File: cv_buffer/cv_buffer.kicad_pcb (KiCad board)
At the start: 2 copper layers, 30 x 8 mm, 8 parts, among them J1 CV connector, J2 Pot connector, U1 HT7550-1, U2 TLV6001UIDBVR

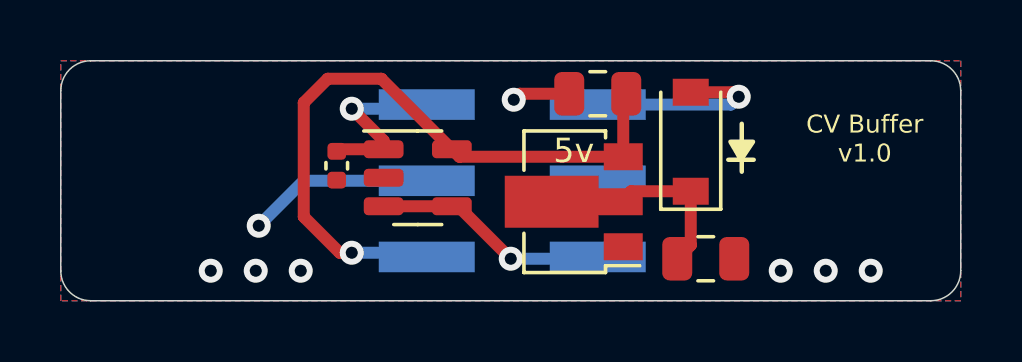
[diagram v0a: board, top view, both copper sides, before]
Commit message: - added tapering resistor - added fabrication script
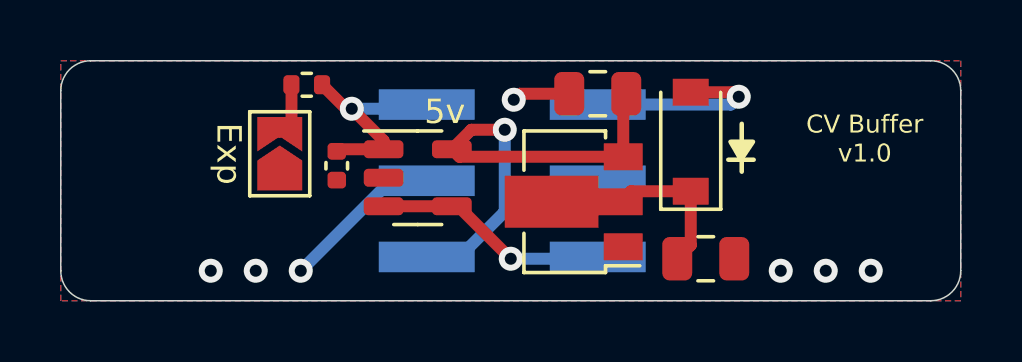
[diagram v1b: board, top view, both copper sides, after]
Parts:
- added JP1: exp shunt, Jumper:SolderJumper-2_P1.3mm_Open_TrianglePad1.0x1.5mm, F.Cu at (173.3, 61.1)
- added R1: 4.7k, Resistor_SMD:R_0402_1005Metric, F.Cu at (174.2, 58.8)
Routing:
- net 5V: track 22.7 -> 15.9 mm
- net Net-(JP1-Pad2): track 0.00 -> 1.74 mm
- net IN: track 5.94 -> 7.26 mm
- net GND: track 8.15 -> 7.38 mm, vias 8 -> 7
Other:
- board text added: "Exp"
- board text removed: "<- Pot Body"

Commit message: Removed taper resistor
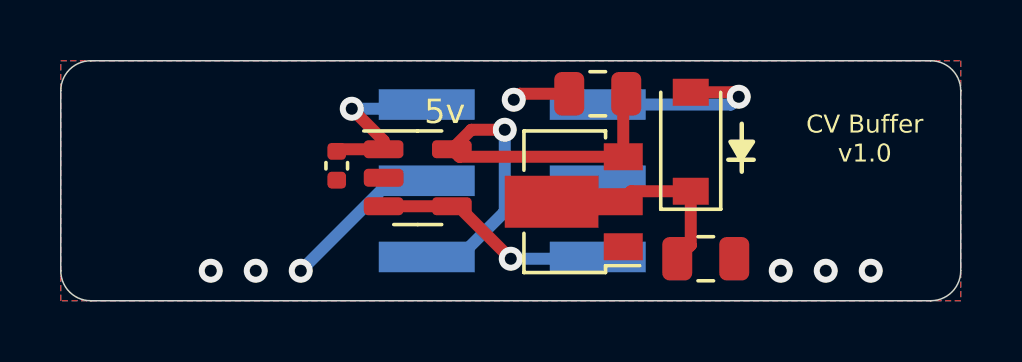
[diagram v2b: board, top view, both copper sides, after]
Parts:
- removed JP1: exp shunt, Jumper:SolderJumper-2_P1.3mm_Open_TrianglePad1.0x1.5mm
- removed R1: 4.7k, Resistor_SMD:R_0402_1005Metric
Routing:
- net Net-(JP1-Pad2): track 1.74 -> 0.00 mm
- net IN: track 7.26 -> 5.94 mm
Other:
- board text removed: "Exp"
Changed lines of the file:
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@@
   (net 5 "V+")
   (net 6 "OUT")
-  (net 7 "Net-(JP1-Pad2)")
-  (footprint "Resistor_SMD:R_0402_1005Metric" (layer "F.Cu")
-    (at 174.2 58.8 180)
-    (descr "Resistor SMD 0402 (1005 Metric), square (rectangular) end terminal, IPC_7351 nominal, (Body size source: IPC-SM-782 page 72, https://www.pcb-3d.com/wordpress/wp-content/uploads/ipc-sm-782a_amendment_1_and_2.pdf), generated with kicad-footprint-generator")
-    (tags "resistor")
-    (property "LCSC" "C25900")
-    (property "Sheetfile" "cv_buffer.kicad_sch")
-    (property "Sheetname" "")
-    (attr smd)
-    (fp_text reference "R1" (at 0 -1.17) (layer "F.SilkS") hide
-      (effects (font (size 1 1) (thickness 0.15)))
-    )
-    (fp_text value "4.7k" (at 0 1.17) (layer "F.Fab")
-      (effects (font (size 1 1) (thickness 0.15)))
-    )
-    (fp_text user "${REFERENCE}" (at 0 0) (layer "F.Fab")
-      (effects (font (size 0.26 0.26) (thickness 0.04)))
-    )
-    (fp_line (start -0.153641 -0.38) (end 0.153641 -0.38) (layer "F.SilkS") (width 0.12))
-    (fp_line (start -0.153641 0.38) (end 0.153641 0.38) (layer "F.SilkS") (width 0.12))
-    (fp_line (start -0.93 0.47) (end -0.93 -0.47) (layer "F.CrtYd") (width 0.05))
-    (fp_line (start 0.93 0.47) (end -0.93 0.47) (layer "F.CrtYd") (width 0.05))
-    (fp_line (start -0.93 -0.47) (end 0.93 -0.47) (layer "F.CrtYd") (width 0.05))
-    (fp_line (start 0.93 -0.47) (end 0.93 0.47) (layer "F.CrtYd") (width 0.05))
-    (fp_line (start -0.525 0.27) (end -0.525 -0.27) (layer "F.Fab") (width 0.1))
-    (fp_line (start 0.525 0.27) (end -0.525 0.27) (layer "F.Fab") (width 0.1))
-    (fp_line (start 0.525 -0.27) (end 0.525 0.27) (layer "F.Fab") (width 0.1))
-    (fp_line (start -0.525 -0.27) (end 0.525 -0.27) (layer "F.Fab") (width 0.1))
-    (pad "1" smd roundrect (at -0.51 0 180) (size 0.54 0.64) (layers "F.Cu" "F.Paste" "F.Mask") (roundrect_rratio 0.25)
-      (net 4 "IN") (pintype "passive"))
-    (pad "2" smd roundrect (at 0.51 0 180) (size 0.54 0.64) (layers "F.Cu" "F.Paste" "F.Mask") (roundrect_rratio 0.25)
-      (net 7 "Net-(JP1-Pad2)") (pintype "passive"))
-    (model "${KICAD6_3DMODEL_DIR}/Resistor_SMD.3dshapes/R_0402_1005Metric.wrl"
-      (offset (xyz 0 0 0))
-      (scale (xyz 1 1 1))
-      (rotate (xyz 0 0 0))
-    )
-  )
   (footprint "Package_TO_SOT_SMD:SOT-23-5" (layer "F.Cu")
     (at 177.9 61.9)
     (descr "SOT, 5 Pin (https://www.jedec.org/sites/default/files/docs/Mo-178c.PDF variant AA), generated with kicad-footprint-generator ipc_gullwing_generator.py")
     (tags "SOT TO_SOT_SMD")
-    (property "Sheetfile" "cv_buffer.kicad_sch")
+    (property "Sheetfile" "File: cv_buffer.kicad_sch")
     (property "Sheetname" "")
     (attr smd)
@@
     (tags "capacitor")
     (property "LCSC" "C15850")
-    (property "Sheetfile" "cv_buffer.kicad_sch")
+    (property "Sheetfile" "File: cv_buffer.kicad_sch")
     (property "Sheetname" "")
     (attr smd)
@@
     (tags "SOD-123")
     (property "LCSC" "C81598")
-    (property "Sheetfile" "cv_buffer.kicad_sch")
+    (property "Sheetfile" "File: cv_buffer.kicad_sch")
     (property "Sheetname" "")
     (attr smd)
@@
     (property "JLCPCB_CORRECTION" "0;0;180")
     (property "LCSC" "C16106")
-    (property "Sheetfile" "cv_buffer.kicad_sch")
+    (property "Sheetfile" "File: cv_buffer.kicad_sch")
     (property "Sheetname" "")
     (attr smd)
@@
     )
   )
-  (footprint "Jumper:SolderJumper-2_P1.3mm_Open_TrianglePad1.0x1.5mm" (layer "F.Cu")
-    (at 173.3 61.1 90)
-    (descr "SMD Solder Jumper, 1x1.5mm Triangular Pads, 0.3mm gap, open")
-    (tags "solder jumper open")
-    (property "Sheetfile" "cv_buffer.kicad_sch")
-    (property "Sheetname" "")
-    (attr exclude_from_pos_files)
-    (fp_text reference "JP1" (at 0 -1.8 90) (layer "F.SilkS") hide
-      (effects (font (size 1 1) (thickness 0.15)))
-    )
-    (fp_text value "exp shunt" (at 0 1.9 90) (layer "F.Fab")
-      (effects (font (size 1 1) (thickness 0.15)))
-    )
-    (fp_line (start 1.4 -1) (end 1.4 1) (layer "F.SilkS") (width 0.12))
-    (fp_line (start 1.4 1) (end -1.4 1) (layer "F.SilkS") (width 0.12))
-    (fp_line (start -1.4 -1) (end 1.4 -1) (layer "F.SilkS") (width 0.12))
-    (fp_line (start -1.4 1) (end -1.4 -1) (layer "F.SilkS") (width 0.12))
-    (fp_line (start 1.65 1.25) (end -1.65 1.25) (layer "F.CrtYd") (width 0.05))
-    (fp_line (start 1.65 1.25) (end 1.65 -1.25) (layer "F.CrtYd") (width 0.05))
-    (fp_line (start -1.65 -1.25) (end 1.65 -1.25) (layer "F.CrtYd") (width 0.05))
-    (fp_line (start -1.65 -1.25) (end -1.65 1.25) (layer "F.CrtYd") (width 0.05))
-    (pad "1" smd custom (at -0.725 0 90) (size 0.3 0.3) (layers "F.Cu" "F.Mask")
-      (net 2 "GND") (pinfunction "A") (pintype "passive") (zone_connect 2)
-      (options (clearance outline) (anchor rect))
-      (primitives
-        (gr_poly (pts
-            (xy 1 0)
-            (xy 0.5 0.75)
-            (xy -0.5 0.75)
-            (xy -0.5 -0.75)
-            (xy 0.5 -0.75)
-          ) (width 0) (fill yes))
-      ))
-    (pad "2" smd custom (at 0.725 0 90) (size 0.3 0.3) (layers "F.Cu" "F.Mask")
-      (net 7 "Net-(JP1-Pad2)") (pinfunction "B") (pintype "passive") (zone_connect 2)
-      (options (clearance outline) (anchor rect))
-      (primitives
-        (gr_poly (pts
-            (xy 0.5 0.75)
-            (xy -0.65 0.75)
-            (xy -0.15 0)
-            (xy -0.65 -0.75)
-            (xy 0.5 -0.75)
-          ) (width 0) (fill yes))
-      ))
-  )
   (footprint "Capacitor_SMD:C_0805_2012Metric" (layer "F.Cu")
     (at 183.9 59.1 180)
@@
     (tags "capacitor")
     (property "LCSC" "C15850")
-    (property "Sheetfile" "cv_buffer.kicad_sch")
+    (property "Sheetfile" "File: cv_buffer.kicad_sch")
     (property "Sheetname" "")
     (attr smd)
@@
     (tags "capacitor")
     (property "LCSC" "C307331")
-    (property "Sheetfile" "cv_buffer.kicad_sch")
+    (property "Sheetfile" "File: cv_buffer.kicad_sch")
     (property "Sheetname" "")
     (attr smd)
@@
   (footprint "cycfi_library:pin_header_1x3p_2.54mm_smd_horizontal" (layer "B.Cu")
     (at 178.2 59.46 180)
-    (property "Sheetfile" "cv_buffer.kicad_sch")
+    (property "Sheetfile" "File: cv_buffer.kicad_sch")
     (property "Sheetname" "")
     (attr through_hole)
@@
   (footprint "cycfi_library:pin_header_1x3p_2.54mm_smd_horizontal" (layer "B.Cu")
     (at 183.9 64.54)
-    (property "Sheetfile" "cv_buffer.kicad_sch")
+    (property "Sheetfile" "File: cv_buffer.kicad_sch")
     (property "Sheetname" "")
     (attr through_hole)
@@
     (effects (font (size 0.6 0.6) (thickness 0.125)))
   )
-  (gr_text "Exp" (at 171.6 61.1 270) (layer "F.SilkS")
-    (effects (font (size 0.8128 0.8128) (thickness 0.1524)))
-  )
   (segment (start 185.0125 62.35) (end 184.6625 62.7) (width 0.4) (layer "F.Cu") (net 1))
   (segment (start 187 64.15) (end 186.55 64.6) (width 0.4) (layer "F.Cu") (net 1))
@@
   (segment (start 176.7625 60.95) (end 175.27 60.95) (width 0.4) (layer "F.Cu") (net 4))
   (segment (start 176.7625 60.95) (end 176.7625 60.6625) (width 0.4) (layer "F.Cu") (net 4))
-  (segment (start 175.51 59.6) (end 174.71 58.8) (width 0.4) (layer "F.Cu") (net 4))
-  (segment (start 175.7 59.6) (end 175.51 59.6) (width 0.4) (layer "F.Cu") (net 4))
   (segment (start 175.27 60.95) (end 175.2 61.02) (width 0.4) (layer "F.Cu") (net 4))
   (segment (start 176.7625 60.6625) (end 175.7 59.6) (width 0.4) (layer "F.Cu") (net 4))
@@
   (segment (start 181 64.6) (end 183.84 64.6) (width 0.4) (layer "B.Cu") (net 6))
   (segment (start 183.84 64.6) (end 183.9 64.54) (width 0.4) (layer "B.Cu") (net 6))
-  (segment (start 173.69 58.8) (end 173.69 59.985) (width 0.4) (layer "F.Cu") (net 7))
-  (segment (start 173.69 59.985) (end 173.3 60.375) (width 0.4) (layer "F.Cu") (net 7))
   (zone (net 2) (net_name "GND") (layer "F.Cu") (hatch edge 0.508)
     (connect_pads (clearance 0.254))

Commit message: CV buffer updates to v3.1 PCB re-layout + various schematic refinements
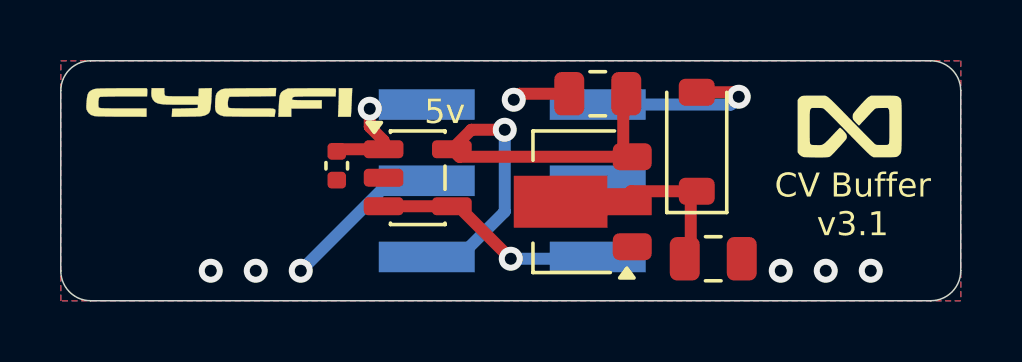
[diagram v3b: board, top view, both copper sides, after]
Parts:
- added G***: LOGO, cycfi_library:cycfi-logo-9mm, F.Cu at (171.2, 59.4)
- added G***: LOGO, cycfi_library:infinity_logo_4mm, F.Cu at (192.3, 60.2)
- J2: value Pot connector -> CV connector
- moved J1 2.54 mm to (183.9, 62.0)
- moved J2 2.54 mm to (178.2, 62.0)
- moved C1 0.25 mm to (187.8, 64.6)
- moved D1 0.20 mm to (187.2, 60.7)
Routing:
- net IN: track 5.94 -> 5.09 mm
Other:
- rule pad_to_mask_clearance: 0.2 -> 0
- board text added: "CV Buffer v3.1"
- board text removed: "CV Buffer v1.0"
- board text removed: "GND"

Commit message: Added output 1k resistor
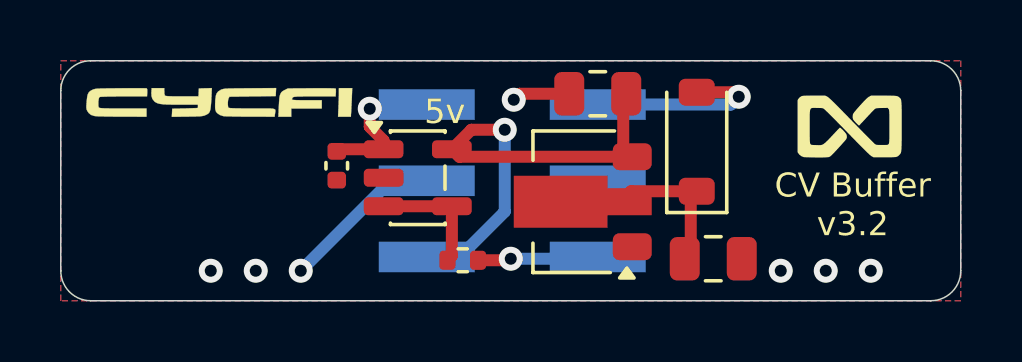
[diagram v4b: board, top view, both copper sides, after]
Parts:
- added R2: 1K, Resistor_SMD:R_0402_1005Metric, F.Cu at (179.4, 64.7)
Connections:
- U2 pad 3: OUT -> Net-(U2--)
- U2 pad 4: OUT -> Net-(U2--)
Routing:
- net Net-(U2--): track 0.00 -> 4.35 mm
- net OUT: track 7.89 -> 4.04 mm
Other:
- board text added: "CV Buffer v3.2"
- board text removed: "CV Buffer v3.1"
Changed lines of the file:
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@@
 	(net 5 "V+")
 	(net 6 "OUT")
+	(net 7 "Net-(U2--)")
 	(footprint "cycfi_library:cycfi-logo-9mm"
 		(layer "F.Cu")
@@
 			(layers "F.Cu" "F.Mask" "F.Paste")
 			(roundrect_rratio 0.25)
-			(net 6 "OUT")
+			(net 7 "Net-(U2--)")
 			(pinfunction "-")
 			(pintype "input")
@@
 			(layers "F.Cu" "F.Mask" "F.Paste")
 			(roundrect_rratio 0.25)
-			(net 6 "OUT")
+			(net 7 "Net-(U2--)")
 			(pintype "output")
 		)
@@
 		)
 	)
+	(footprint "Resistor_SMD:R_0402_1005Metric"
+		(layer "F.Cu")
+		(at 179.4 64.65)
+		(descr "Resistor SMD 0402 (1005 Metric), square (rectangular) end terminal, IPC-7351 nominal, (Body size source: IPC-SM-782 page 72, https://www.pcb-3d.com/wordpress/wp-content/uploads/ipc-sm-782a_amendment_1_and_2.pdf), generated with kicad-footprint-generator")
+		(tags "resistor")
+		(property "Reference" "R2"
+			(at 0 -1.17 0)
+			(layer "F.SilkS")
+			(hide yes)
+			(effects
+				(font
+					(size 1 1)
+					(thickness 0.15)
+				)
+			)
+		)
+		(property "Value" "1K"
+			(at 0 1.17 0)
+			(layer "F.Fab")
+			(effects
+				(font
+					(size 1 1)
+					(thickness 0.15)
+				)
+			)
+		)
+		(property "Datasheet" "~"
+			(at 0 0 0)
+			(layer "F.Fab")
+			(hide yes)
+			(effects
+				(font
+					(size 1.27 1.27)
+					(thickness 0.15)
+				)
+			)
+		)
+		(property "Description" ""
+			(at 0 0 0)
+			(layer "F.Fab")
+			(hide yes)
+			(effects
+				(font
+					(size 1.27 1.27)
+					(thickness 0.15)
+				)
+			)
+		)
+		(property "LCSC" "C11702"
+			(at 0 0 0)
+			(unlocked yes)
+			(layer "F.Fab")
+			(hide yes)
+			(effects
+				(font
+					(size 1 1)
+					(thickness 0.15)
+				)
+			)
+		)
+		(property ki_fp_filters "R_*")
+		(sheetname "/")
+		(sheetfile "cv_buffer.kicad_sch")
+		(attr smd)
+		(fp_line
+			(start -0.153641 -0.38)
+			(end 0.153641 -0.38)
+			(stroke
+				(width 0.12)
+				(type solid)
+			)
+			(layer "F.SilkS")
+		)
+		(fp_line
+			(start -0.153641 0.38)
+			(end 0.153641 0.38)
+			(stroke
+				(width 0.12)
+				(type solid)
+			)
+			(layer "F.SilkS")
+		)
+		(fp_rect
+			(start -0.93 -0.47)
+			(end 0.93 0.47)
+			(stroke
+				(width 0.05)
+				(type solid)
+			)
+			(fill no)
+			(layer "F.CrtYd")
+		)
+		(fp_rect
+			(start -0.525 -0.27)
+			(end 0.525 0.27)
+			(stroke
+				(width 0.1)
+				(type solid)
+			)
+			(fill no)
+			(layer "F.Fab")
+		)
+		(fp_text user "${REFERENCE}"
+			(at 0 0 0)
+			(layer "F.Fab")
+			(effects
+				(font
+					(size 0.26 0.26)
+					(thickness 0.04)
+				)
+			)
+		)
+		(pad "1" smd roundrect
+			(at -0.51 0)
+			(size 0.54 0.64)
+			(layers "F.Cu" "F.Mask" "F.Paste")
+			(roundrect_rratio 0.25)
+			(net 7 "Net-(U2--)")
+			(pintype "passive")
+		)
+		(pad "2" smd roundrect
+			(at 0.51 0)
+			(size 0.54 0.64)
+			(layers "F.Cu" "F.Mask" "F.Paste")
+			(roundrect_rratio 0.25)
+			(net 6 "OUT")
+			(pintype "passive")
+		)
+		(embedded_fonts no)
+		(model "${KICAD9_3DMODEL_DIR}/Resistor_SMD.3dshapes/R_0402_1005Metric.step"
+			(offset
+				(xyz 0 0 0)
+			)
+			(scale
+				(xyz 1 1 1)
+			)
+			(rotate
+				(xyz 0 0 0)
+			)
+		)
+	)
 	(footprint "cycfi_library:pin_header_1x3p_2.54mm_smd_horizontal"
 		(layer "B.Cu")
@@
 		)
 	)
-	(gr_text "CV Buffer\nv3.1"
+	(gr_text "CV Buffer\nv3.2"
 		(at 192.4 62.8 0)
 		(layer "F.SilkS")
@@
 	)
 	(segment
-		(start 179.0375 62.85)
-		(end 179.25 62.85)
-		(width 0.4)
+		(start 180.95 64.65)
+		(end 181 64.6)
+		(width 0.25)
 		(layer "F.Cu")
 		(net 6)
 	)
 	(segment
-		(start 179.25 62.85)
-		(end 181 64.6)
-		(width 0.4)
-		(layer "F.Cu")
-		(net 6)
-	)
-	(segment
-		(start 176.7625 62.85)
-		(end 179.0375 62.85)
+		(start 179.91 64.65)
+		(end 180.95 64.65)
 		(width 0.4)
 		(layer "F.Cu")
@@
 		(net 6)
 	)
+	(segment
+		(start 179.0375 62.85)
+		(end 179.25 62.85)
+		(width 0.4)
+		(layer "F.Cu")
+		(net 7)
+	)
+	(segment
+		(start 179.0375 62.85)
+		(end 179.0375 64.5025)
+		(width 0.4)
+		(layer "F.Cu")
+		(net 7)
+	)
+	(segment
+		(start 179.0375 64.5025)
+		(end 178.89 64.65)
+		(width 0.4)
+		(layer "F.Cu")
+		(net 7)
+	)
+	(segment
+		(start 176.7625 62.85)
+		(end 179.0375 62.85)
+		(width 0.4)
+		(layer "F.Cu")
+		(net 7)
+	)
 	(zone
